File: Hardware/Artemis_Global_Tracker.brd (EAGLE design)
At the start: 50.8 x 63.5 mm, 203 parts, among them J1 IRIDIUM_9603N, J2 USB-C, J6 U.FL, J7 ANTENNA-GROUNDEDEDGE_SMA, Q1 DMG3414U-7, Q2 DMG3415U-7, Q3 DMG3415U-7, Q4 600mA/40V, U1 CH340E_MSOP10, U10 3.3V, U2 LTC3225EDDB#TRMPBF, U3 ADM4210-1, U4 UBLOX_ZOE_M8-0-10, U5 AS179-92LF, U6 MS8607-02BA01, U7 ARTEMIS_MODULESMD, U8 V_SUPERVISORBD48K24G-TL, U9 MCP73831, X1 32.768kHz, X2 32.768kHz

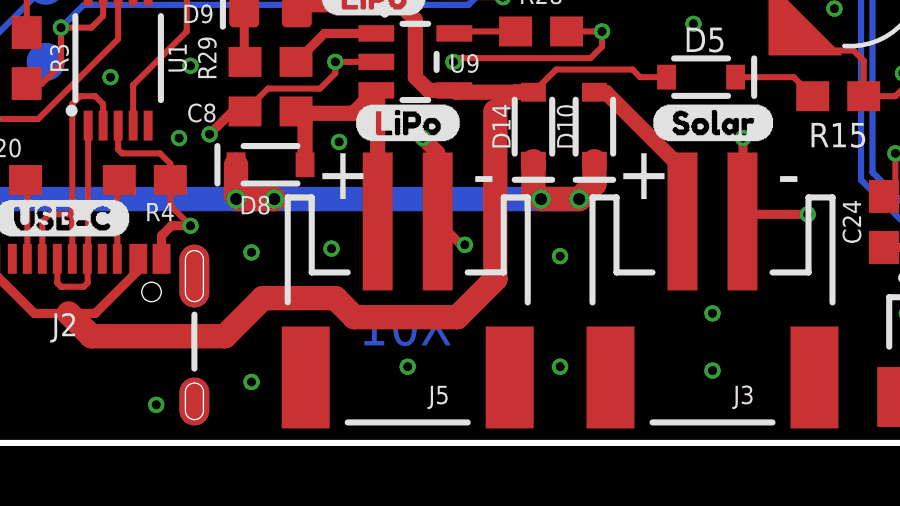
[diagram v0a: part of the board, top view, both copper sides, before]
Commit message: More name changes and updates to the Message Fields definition
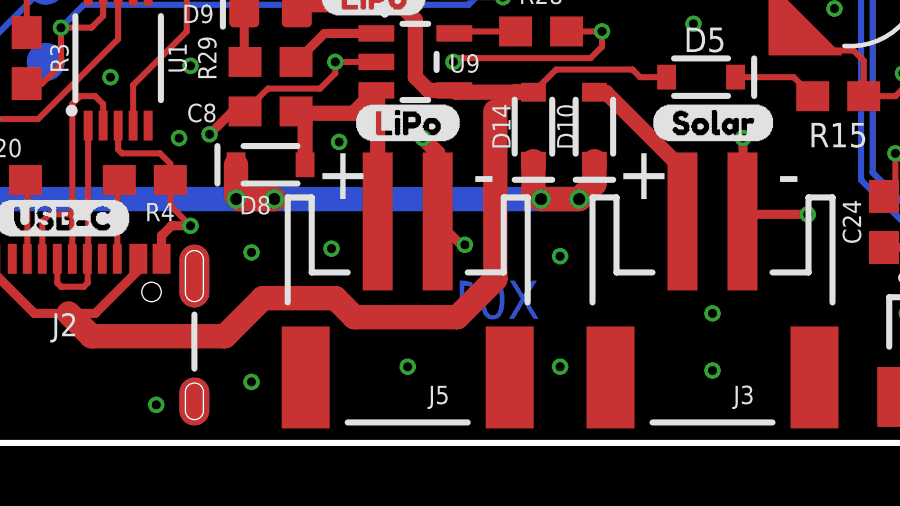
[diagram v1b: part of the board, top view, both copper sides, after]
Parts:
- U$41: device IRIDIUM:IRIDIUM0 -> GLOBAL_0.05:GLOBAL0
- moved U$41 0.25 mm to (30.1, 12.2)
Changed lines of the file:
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@@
 <wire x1="50.8" y1="63.5" x2="50.8" y2="0" width="0.2032" layer="20"/>
 <wire x1="50.8" y1="0" x2="0" y2="0" width="0.2032" layer="20"/>
-<text x="22.1742" y="3.8862" size="1.27" layer="16" font="vector" ratio="15" rot="MR0" align="center">X01</text>
+<text x="25.0952" y="4.7752" size="1.27" layer="16" font="vector" ratio="15" rot="MR0" align="center">X01</text>
 <text x="27.01925" y="50.26025" size="1.778" layer="22" ratio="18" rot="MR90" align="bottom-center">-</text>
 <text x="32.766" y="49.2125" size="1.778" layer="22" ratio="18" rot="MR0" align="bottom-center">+</text>
@@
 <element name="U$39" library="TX1" package="TX10" value="" x="19.685" y="43.18" smashed="yes" rot="MR0"/>
 <element name="U$40" library="ARTEMIS" package="ARTEMIS0" value="" x="30.48" y="14.605" smashed="yes" rot="MR0"/>
-<element name="U$41" library="IRIDIUM" package="IRIDIUM0" value="" x="29.845" y="12.192" smashed="yes" rot="MR0"/>
+<element name="U$41" library="GLOBAL_0.05" package="GLOBAL0" value="" x="30.099" y="12.192" smashed="yes" rot="MR0"/>
 <element name="U$42" library="TRACKER" package="TRACKER0" value="" x="30.607" y="9.779" smashed="yes" rot="MR0"/>
 <element name="U$43" library="PWR_LED" package="PWR_LED0" value="" x="50.419" y="15.748" smashed="yes" rot="MR0"/>

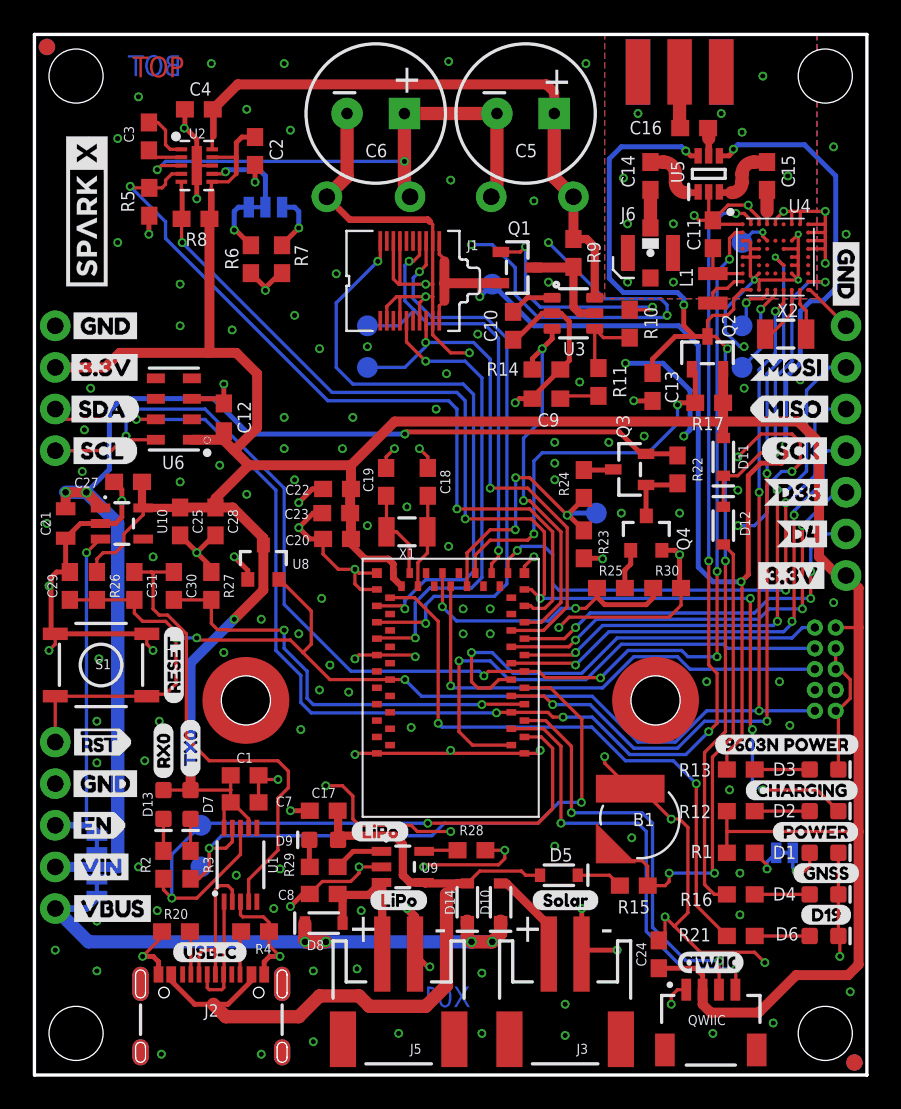
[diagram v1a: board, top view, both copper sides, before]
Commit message: PROD_ID updates
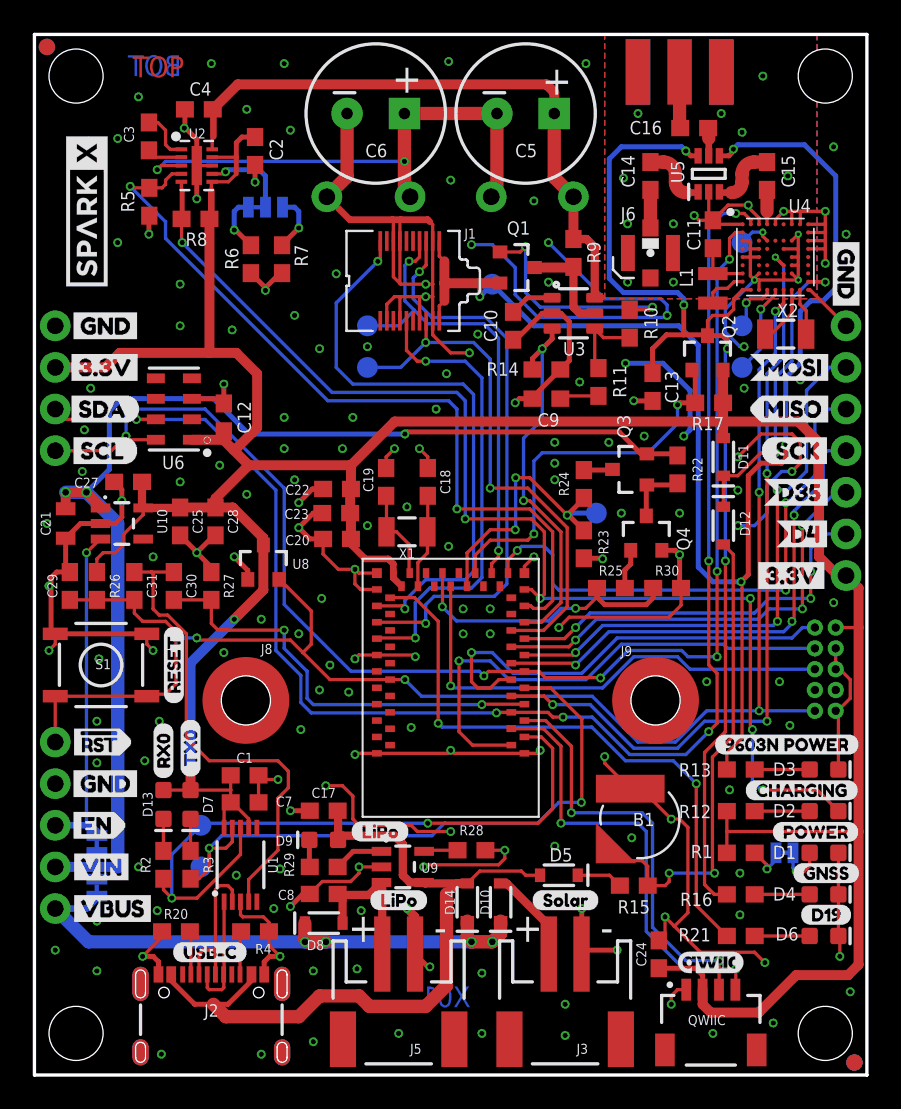
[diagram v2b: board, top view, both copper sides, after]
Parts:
- added J8, J9: STANDOFFS_M2X0.4_STEEL_6MM, New_Parts:STANDOFF_M2X0.4
- C5, C6: device SparkFun-Capacitors:CPOL-RADIAL-1F-2.7V -> New_Parts:CPOL-RADIAL-1F-2.7V
- Q1: value DMG3414U-7 -> 5.8A/30V/35mΩ; device New_Parts:SOT23-R -> SparkFun-DiscreteSemi:SOT23-3
- Q2, Q3: value DMG3415U-7 -> 20V/4.2A/52mΩ/1.4W; device New_Parts:SOT23-R -> SparkFun-DiscreteSemi:SOT23-3
- U4: value UBLOX_ZOE_M8-0-10 -> U-BLOX_ZOE_M8Q-0-10
- moved J1 27.5 mm to (22.9, 48.5)
- moved Q2 0.05 mm to (41.1, 44.0)
- moved Q1 0.05 mm to (29.4, 49.3)
- moved Q3 0.05 mm to (36.4, 37.0)
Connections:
- net GND: now also J8.1, J9.1; no longer J1.HOLE1, J1.HOLE2
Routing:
- net GND: track 311.3 -> 313.7 mm
